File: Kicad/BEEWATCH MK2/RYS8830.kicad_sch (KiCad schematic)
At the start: 33 parts, among them IC1 LTC3549EDCB#TRMPBF, Q4 DMG6968U, Q5 BSS138, Q6 BSS138, Q7 BSS138, Q8 DMP1045U-7, U7 RYS8830

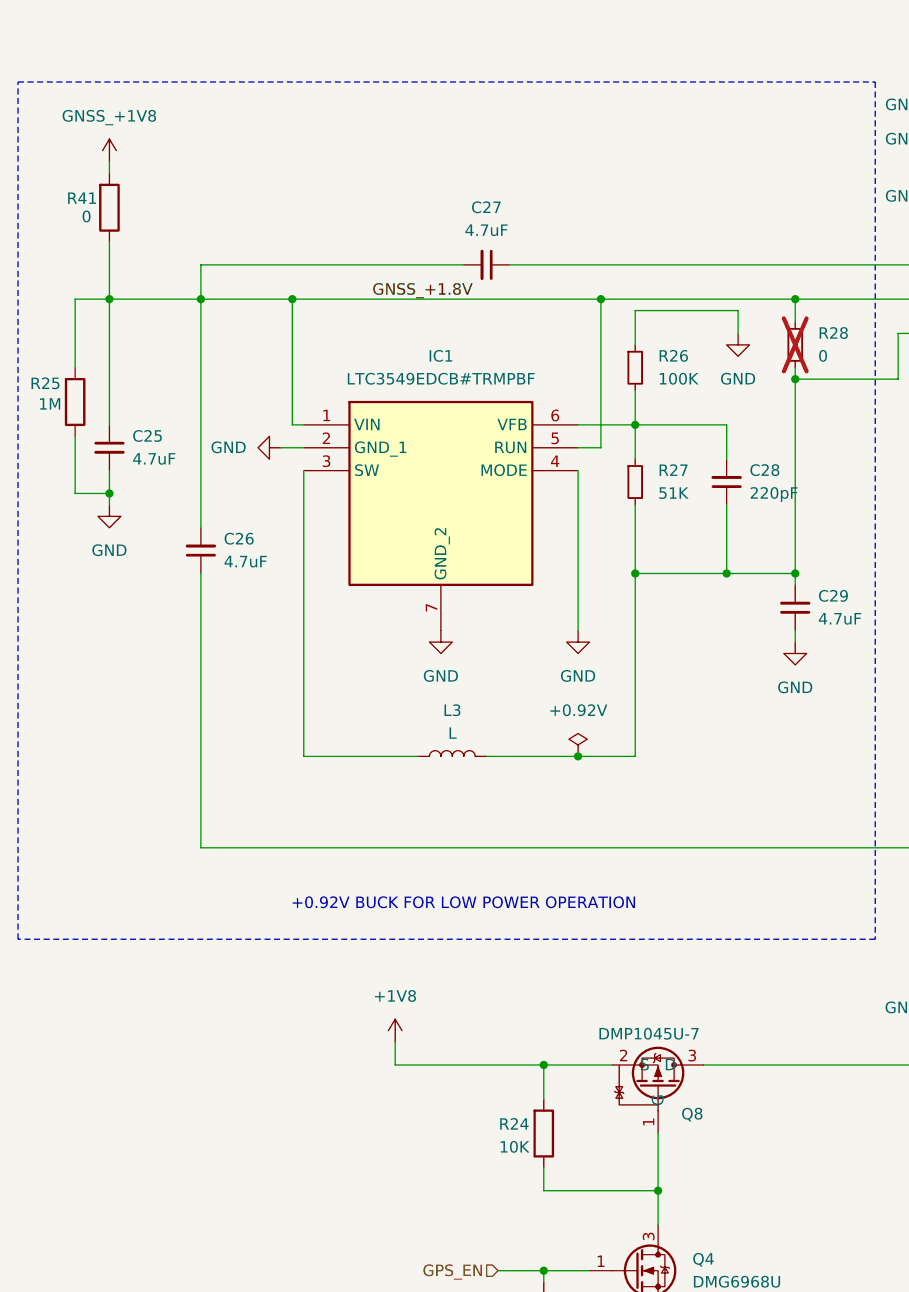
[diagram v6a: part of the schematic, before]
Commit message: ERC going on anf All Lib issue is fixed
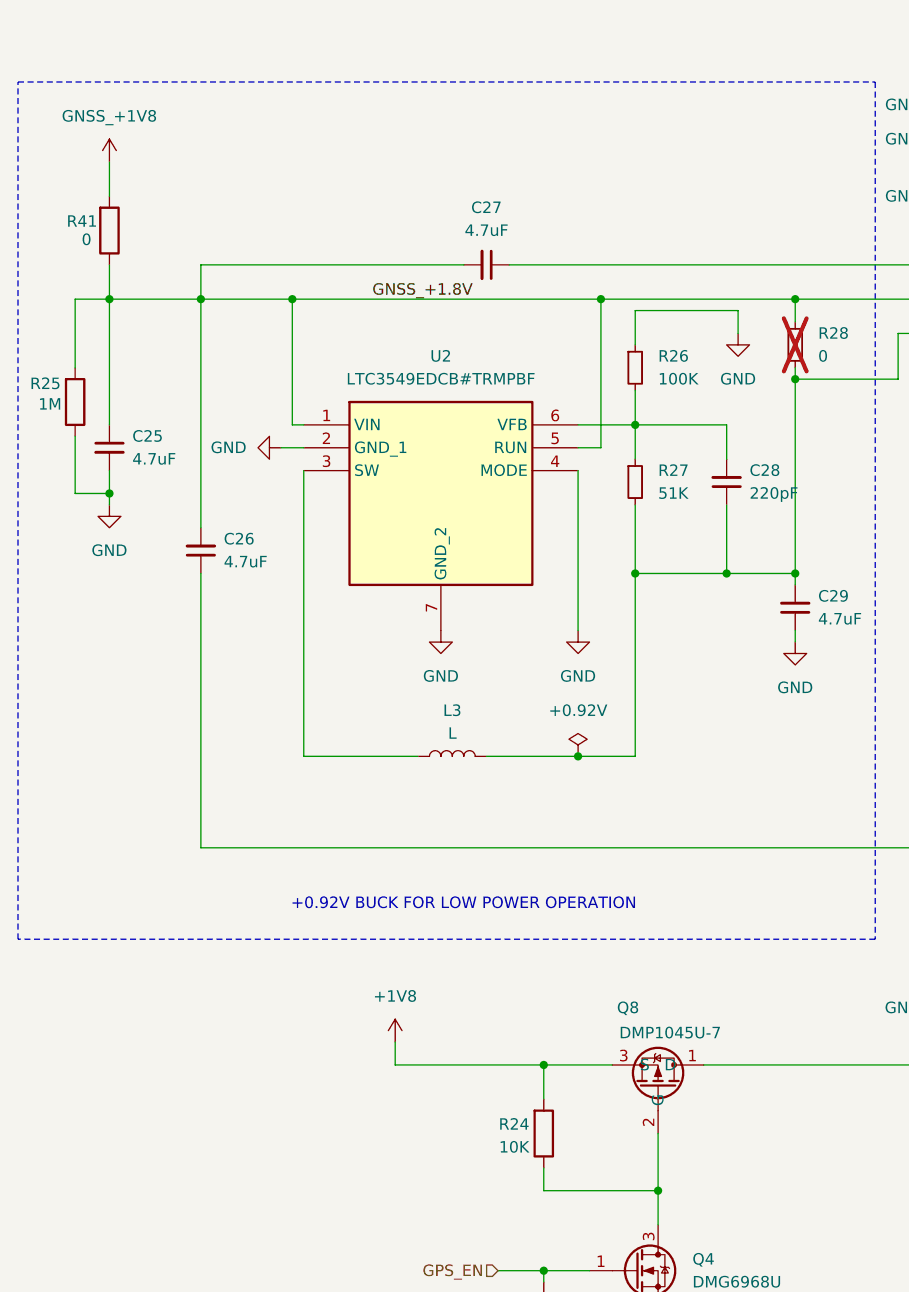
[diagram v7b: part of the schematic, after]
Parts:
- removed IC1: LTC3549EDCB#TRMPBF, Package_DFN_QFN:DFN-6-1EP_3x2mm_P0.5mm_EP1.65x1.35mm, symbol LTC3549EDCB#TRMPBF:LTC3549EDCB#TRMPBF
- removed Q8: DMP1045U-7, Package_TO_SOT_SMD:SOT-23-3, symbol Project_Library:DMP1045U-7
- added Q8: DMP1045U-7, Package_TO_SOT_SMD:SOT-23-3, symbol SM_PMOS:DMP1045U-7
- added U2: LTC3549EDCB#TRMPBF, Package_DFN_QFN:DFN-6-1EP_3x2mm_P0.5mm_EP1.65x1.35mm, symbol SM_BUCK:LTC3549EDCB#TRMPBF
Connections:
- net +1V8: now also Q8.3 (S)
- net GND: now also U2.2 (GND_1), U2.4 (MODE), U2.7 (GND_2)
- net GNSS_+1.8V: now also U2.1 (VIN), U2.5 (RUN)
- net GNSS_+1V8: now also Q8.1 (D)
- net at Q4.3 (D), R24.1: now also Q8.2 (G)
- net at L3.1: now also U2.3 (SW)
- net at C28.2, R26.2, R27.1: now also U2.6 (VFB)
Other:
- moved on the sheet: R41
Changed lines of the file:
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@@
 	(wire
 		(pts
-			(xy 30.48 53.34) (xy 30.48 54.61)
+			(xy 30.48 53.34) (xy 30.48 57.15)
 		)
 		(stroke
@@
 	(wire
 		(pts
-			(xy 30.48 62.23) (xy 30.48 68.58)
+			(xy 30.48 64.77) (xy 30.48 68.58)
 		)
 		(stroke
@@
 	)
 	(symbol
+		(lib_id "SM_PMOS:DMP1045U-7")
+		(at 91.44 153.67 270)
+		(mirror x)
+		(unit 1)
+		(exclude_from_sim no)
+		(in_bom yes)
+		(on_board yes)
+		(dnp no)
+		(property "Reference" "Q8"
+			(at 86.868 147.32 90)
+			(effects
+				(font
+					(size 1.27 1.27)
+				)
+				(justify left)
+			)
+		)
+		(property "Value" "DMP1045U-7"
+			(at 87.122 150.114 90)
+			(effects
+				(font
+					(size 1.27 1.27)
+				)
+				(justify left)
+			)
+		)
+		(property "Footprint" "Package_TO_SOT_SMD:SOT-23-3"
+			(at 91.44 153.67 0)
+			(effects
+				(font
+					(size 1.27 1.27)
+				)
+				(hide yes)
+			)
+		)
+		(property "Datasheet" ""
+			(at 91.44 153.67 0)
+			(effects
+				(font
+					(size 1.27 1.27)
+				)
+				(hide yes)
+			)
+		)
+		(property "Description" ""
+			(at 91.44 153.67 0)
+			(effects
+				(font
+					(size 1.27 1.27)
+				)
+				(hide yes)
+			)
+		)
+		(pin "1"
+		)
+		(pin "3"
+		)
+		(pin "2"
+		)
+		(instances
+			(project ""
+				(path "/e9c5fb53-480b-4989-8495-a3341ee99514/33dec73c-f7ec-4dd7-9d85-ef473e07baa9"
+					(reference "Q8")
+					(unit 1)
+				)
+			)
+		)
+	)
+	(symbol
 		(lib_id "Device:C_Small")
 		(at 40.64 96.52 180)
@@
 	)
 	(symbol
-		(lib_id "Project_Library:DMP1045U-7")
-		(at 91.44 157.48 270)
-		(mirror x)
-		(unit 1)
-		(exclude_from_sim no)
-		(in_bom yes)
-		(on_board yes)
-		(dnp no)
-		(property "Reference" "Q8"
-			(at 95.25 159.131 90)
-			(effects
-				(font
-					(size 1.27 1.27)
-				)
-			)
-		)
-		(property "Value" "DMP1045U-7"
-			(at 90.424 150.241 90)
-			(effects
-				(font
-					(size 1.27 1.27)
-				)
-			)
-		)
-		(property "Footprint" "Package_TO_SOT_SMD:SOT-23-3"
-			(at 107.95 154.94 0)
-			(effects
-				(font
-					(size 1.27 1.27)
-				)
-				(hide yes)
-			)
-		)
-		(property "Datasheet" ""
-			(at 95.25 158.75 0)
-			(effects
-				(font
-					(size 1.27 1.27)
-				)
-				(hide yes)
-			)
-		)
-		(property "Description" ""
-			(at 91.44 157.48 0)
-			(effects
-				(font
-					(size 1.27 1.27)
-				)
-				(hide yes)
-			)
-		)
-		(pin "1"
-		)
-		(pin "2"
-		)
-		(pin "3"
-		)
-		(instances
-			(project "BEEWATCH MK3"
-				(path "/e9c5fb53-480b-4989-8495-a3341ee99514/33dec73c-f7ec-4dd7-9d85-ef473e07baa9"
-					(reference "Q8")
-					(unit 1)
-				)
-			)
-		)
-	)
-	(symbol
 		(lib_id "Device:C_Small")
 		(at 106.68 102.87 180)
@@
 	)
 	(symbol
+		(lib_id "SM_BUCK:LTC3549EDCB#TRMPBF")
+		(at 66.04 80.01 0)
+		(unit 1)
+		(exclude_from_sim no)
+		(in_bom yes)
+		(on_board yes)
+		(dnp no)
+		(fields_autoplaced yes)
+		(property "Reference" "U2"
+			(at 67.31 74.93 0)
+			(effects
+				(font
+					(size 1.27 1.27)
+				)
+			)
+		)
+		(property "Value" "LTC3549EDCB#TRMPBF"
+			(at 67.31 77.47 0)
+			(effects
+				(font
+					(size 1.27 1.27)
+				)
+			)
+		)
+		(property "Footprint" "Package_DFN_QFN:DFN-6-1EP_3x2mm_P0.5mm_EP1.65x1.35mm"
+			(at 66.04 80.01 0)
+			(effects
+				(font
+					(size 1.27 1.27)
+				)
+				(hide yes)
+			)
+		)
+		(property "Datasheet" "Datasheet https://www.analog.com/media/en/technical-documentation/data-sheets/3549f.pdf 0 0 Left Top 0 0  Description Linear Technology LTC3549EDCB#TRMPBF, Step Down Buck Boost Switching Regulator, 250mA, Adjustable 0 0 Center Center 0 0  Height 0.8 0 0 Left Top 0 0  Mouser Part Number 584-C3549EDCBTRMPBF 0 0 Left Top 0 0  Mouser Price/Stock https://www.mouser.co.uk/ProductDetail/Analog-Devices/LTC3549EDCBTRMPBF?qs=hVkxg5c3xu%2Ft3z%252BtqK2sZA%3D%3D 0 0 Left Top 0 0  Manufacturer_Name Analog Devices 0 0 Left Top 0 0  Manufacturer_Part_Number LTC3549EDCB#TRMPBF 0 0 Left Top 0 0"
+			(at 66.04 80.01 0)
+			(effects
+				(font
+					(size 1.27 1.27)
+				)
+				(hide yes)
+			)
+		)
+		(property "Description" ""
+			(at 66.04 80.01 0)
+			(effects
+				(font
+					(size 1.27 1.27)
+				)
+				(hide yes)
+			)
+		)
+		(pin "4"
+		)
+		(pin "2"
+		)
+		(pin "3"
+		)
+		(pin "7"
+		)
+		(pin "1"
+		)
+		(pin "6"
+		)
+		(pin "5"
+		)
+		(instances
+			(project ""
+				(path "/e9c5fb53-480b-4989-8495-a3341ee99514/33dec73c-f7ec-4dd7-9d85-ef473e07baa9"
+					(reference "U2")
+					(unit 1)
+				)
+			)
+		)
+	)
+	(symbol
 		(lib_id "Device:R")
 		(at 208.28 90.17 0)
@@
 	(symbol
 		(lib_id "Device:R")
-		(at 30.48 58.42 0)
+		(at 30.48 60.96 0)
 		(mirror x)
 		(unit 1)
@@
 		(dnp no)
 		(property "Reference" "R41"
-			(at 27.432 57.404 0)
+			(at 27.432 59.944 0)
 			(effects
 				(font
@@
 		)
 		(property "Value" "0"
-			(at 27.94 59.436 0)
+			(at 27.94 61.976 0)
 			(effects
 				(font
@@
 		)
 		(property "Footprint" "Resistor_SMD:R_0402_1005Metric_Pad0.72x0.64mm_HandSolder"
-			(at 28.702 58.42 90)
+			(at 28.702 60.96 90)
 			(effects
 				(font
@@
 		)
 		(property "Datasheet" "~"
-			(at 30.48 58.42 0)
+			(at 30.48 60.96 0)
 			(effects
 				(font
@@
 		)
 		(property "Description" "Resistor"
-			(at 30.48 58.42 0)
+			(at 30.48 60.96 0)
 			(effects
 				(font
@@
 					(unit 1)
 				)
-			)
-		)
-	)
-	(symbol
-		(lib_id "LTC3549EDCB#TRMPBF:LTC3549EDCB#TRMPBF")
-		(at 52.07 82.55 0)
-		(unit 1)
-		(exclude_from_sim no)
-		(in_bom yes)
-		(on_board yes)
-		(dnp no)
-		(fields_autoplaced yes)
-		(property "Reference" "IC1"
-			(at 67.31 74.93 0)
-			(effects
-				(font
-					(size 1.27 1.27)
-				)
-			)
-		)
-		(property "Value" "LTC3549EDCB#TRMPBF"
-			(at 67.31 77.47 0)
-			(effects
-				(font
-					(size 1.27 1.27)
-				)
-			)
-		)
-		(property "Footprint" "Package_DFN_QFN:DFN-6-1EP_3x2mm_P0.5mm_EP1.65x1.35mm"
-			(at 78.74 177.47 0)
-			(effects
-				(font
-					(size 1.27 1.27)
-				)
-				(justify left top)
-				(hide yes)
-			)
-		)
-		(property "Datasheet" "https://www.analog.com/media/en/technical-documentation/data-sheets/3549f.pdf"
-			(at 78.74 277.47 0)
-			(effects
-				(font
-					(size 1.27 1.27)
-				)
-				(justify left top)
-				(hide yes)
-			)
-		)
-		(property "Description" "Linear Technology LTC3549EDCB#TRMPBF, Step Down Buck Boost Switching Regulator, 250mA, Adjustable"
-			(at 52.07 82.55 0)
-			(effects
-				(font
-					(size 1.27 1.27)
-				)
-				(hide yes)
-			)
-		)
-		(property "Height" "0.8"
-			(at 78.74 477.47 0)
-			(effects
-				(font
-					(size 1.27 1.27)
-				)
-				(justify left top)
-				(hide yes)
-			)
-		)
-		(property "Mouser Part Number" "584-C3549EDCBTRMPBF"
-			(at 78.74 577.47 0)
-			(effects
-				(font
-					(size 1.27 1.27)
-				)
-				(justify left top)
-				(hide yes)
-			)
-		)
-		(property "Mouser Price/Stock" "https://www.mouser.co.uk/ProductDetail/Analog-Devices/LTC3549EDCBTRMPBF?qs=hVkxg5c3xu%2Ft3z%252BtqK2sZA%3D%3D"
-			(at 78.74 677.47 0)
-			(effects
-				(font
-					(size 1.27 1.27)
-				)
-				(justify left top)
-				(hide yes)
-			)
-		)
-		(property "Manufacturer_Name" "Analog Devices"
-			(at 78.74 777.47 0)
-			(effects
-				(font
-					(size 1.27 1.27)
-				)
-				(justify left top)
-				(hide yes)
-			)
-		)
-		(property "Manufacturer_Part_Number" "LTC3549EDCB#TRMPBF"
-			(at 78.74 877.47 0)
-			(effects
-				(font
-					(size 1.27 1.27)
-				)
-				(justify left top)
-				(hide yes)
-			)
-		)
-		(pin "7"
-		)
-		(pin "3"
-		)
-		(pin "5"
-		)
-		(pin "1"
-		)
-		(pin "2"
-		)
-		(pin "6"
-		)
-		(pin "4"
-		)
-		(instances
-			(project ""
-				(path "/e9c5fb53-480b-4989-8495-a3341ee99514/33dec73c-f7ec-4dd7-9d85-ef473e07baa9"
-					(reference "IC1")
-					(unit 1)
-				)

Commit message: Deep optmization 90% completed
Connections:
- net +0.92V: now reaches C28.1, C29.2, L3.2, R27.2, R28.2, R49.1
- net SW: now reaches L3.1, U2.3 (SW)
- net FB: now reaches C28.2, R26.2, R27.1, U2.6 (VFB)
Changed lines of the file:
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@@
+	)
+	(junction
+		(at 88.9 119.38)
+		(diameter 0)
+		(color 0 0 0 0)
 	)
 	(junction
@@
 	(junction
 		(at 106.68 99.06)
-		(diameter 0)
-		(color 0 0 0 0)
-	)
-	(junction
-		(at 82.55 119.38)
 		(diameter 0)
 		(color 0 0 0 0)
@@
 	(wire
 		(pts
-			(xy 72.39 119.38) (xy 82.55 119.38)
+			(xy 72.39 119.38) (xy 88.9 119.38)
 		)
 		(stroke
@@
 		(pts
 			(xy 106.68 99.06) (xy 106.68 100.33)
-		)
-		(stroke
-			(width 0)
-			(type default)
-		)
-	)
-	(wire
-		(pts
-			(xy 82.55 119.38) (xy 88.9 119.38)
 		)
 		(stroke
@@
 		)
 	)
+	(label "RUN"
+		(at 85.09 77.47 90)
+		(effects
+			(font
+				(size 1.27 1.27)
+			)
+			(justify left bottom)
+		)
+	)
+	(label "FB"
+		(at 92.71 82.55 0)
+		(effects
+			(font
+				(size 1.27 1.27)
+			)
+			(justify left bottom)
+		)
+	)
+	(label "SW"
+		(at 52.07 106.68 90)
+		(effects
+			(font
+				(size 1.27 1.27)
+			)
+			(justify left bottom)
+		)
+	)
 	(label "GNSS_+1.8V"
 		(at 163.83 104.14 270)
@@
 			)
 			(justify right bottom)
+		)
+	)
+	(label "+0.92V"
+		(at 77.47 119.38 0)
+		(effects
+			(font
+				(size 1.27 1.27)
+			)
+			(justify left bottom)
 		)
 	)
@@
 	(symbol
 		(lib_id "power:PWR_FLAG")
-		(at 82.55 119.38 0)
+		(at 88.9 119.38 270)
 		(unit 1)
 		(exclude_from_sim no)
@@
 		(fields_autoplaced yes)
 		(property "Reference" "#FLG01"
-			(at 82.55 117.475 0)
+			(at 90.805 119.38 0)
 			(effects
 				(font
@@
 		)
 		(property "Value" "+0.92V"
-			(at 82.55 114.3 0)
+			(at 92.71 119.3799 90)
 			(effects
 				(font
 					(size 1.27 1.27)
 				)
+				(justify left)
 			)
 		)
 		(property "Footprint" ""
-			(at 82.55 119.38 0)
+			(at 88.9 119.38 0)
 			(effects
 				(font
@@
 		)
 		(property "Datasheet" "~"
-			(at 82.55 119.38 0)
+			(at 88.9 119.38 0)
 			(effects
 				(font
@@
 		)
 		(property "Description" "Special symbol for telling ERC where power comes from"
-			(at 82.55 119.38 0)
+			(at 88.9 119.38 0)
 			(effects
 				(font
